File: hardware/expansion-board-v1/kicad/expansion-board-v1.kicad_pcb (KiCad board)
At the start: 4 copper layers, 100 x 62 mm, 156 parts, among them J1 PinHeader_2x20_P2.54mm_Vertic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, J2 U.FL_Hirose_U.FL-R-SMT-1_Vert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, J4 USB_C_Receptacle_HRO_TYPE-C-3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, J5 U.FL_Hirose_U.FL-R-SMT-1_Vert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, J6 U.FL_Hirose_U.FL-R-SMT-1_Vert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, J7 ANT_IFA_1090MHz, J8 U.FL_Hirose_U.FL-R-SMT-1_Vert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, Q2 SOT-23, Q3 SOT-23, Q4 SOT-23, Q5 SOT-23, SW1 SolderJumper-2_P1.3mm_Open_Pa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, SW2 SolderJumper-2_P1.3mm_Open_Pa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, U1 SOT-23-5, U10 QFN-48-1EP_7x7mm_P0.5mm_EP5.1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, U11 DFN-8-1EP_2x2mm_P0.5mm_EP0.86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, U12 SOT-363_SC-70-6, U13 AD8319_LFCSP-8-EP, U14 MSOP-8_3x3mm_P0.65mm, U15 SOT-23-6, U16 SOT-363_SC-70-6, U17 SOT-363_SC-70-6, U2 SOT-23-5, U3 SOT-23-5, U4 BNO085_LGA-28, U5 BMP388_LGA-10, U6 LGA-16_3x3mm_P0.5mm, U7 ATGM336H_LCC-18, U8 QFN-56-1EP_7x7mm_P0.4mm_EP3.2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, U9 SOIC-8_5.3x5.3mm_P1.27mm, Y1 Crystal_SMD_3225-4Pin_3.2x2.5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, Y2 Crystal_SMD_3225-4Pin_3.2x2.5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, Y3 Crystal_SMD_3215-2Pin_3.2x1.5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

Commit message: feat(hw): 布局冻结为设计数据 + 丝印对齐机检 + 板名改 Avionics Board
## 布局所有权转移
区域装箱器的任务已完成——它把 152 个元件从零摆到可用起点。
用户人工精修了 81 个元件（把 CC1312R 去耦聚拢、978 直流侧贴近 J1 等，
装箱器摆不出来的判断）。精修后坐标即设计本身，不该再被算法覆盖。

  tools/export_placement.py  读 PCB → 行吸附 → 产出 PLACEMENT.py（只读源板）
  tools/PLACEMENT.py         156 元件 + 156 位号坐标，**设计数据不是生成物**
  gen_pcb.py / gen_silk.py   改为按 PLACEMENT.py 摆位；装箱与试位降级为新件兜底

往返验证：139/156 逐值一致，17 处差异恰为吸附项，无意外漂移。

## 对齐吸附（人工对不准，必须靠算法）
判据：同簇 = y 差 ≤0.35mm 且 x 间距 ≤12mm；目标取众数而非中位数
（多数已对齐、少数漂了，中位数会把对好的拽歪）。
实例：用户手拉 L14 行到 66.500，而 Q5 行是 66.553——肉眼差了 0.053mm。

## 新增三道丝印机检（这些问题此前靠人眼发现，漏过多次）
- 位号不得压在自己元件本体上（大件豁免）
- 同行 + 同高 + 同侧的位号绝对 y 必须一致
- 行对齐 pass 的每个候选位置都要过 压本体/压焊盘/压文字 三项

## 修掉的缺陷
- 冻结时把**失败状态**也固化：F.Fab 与"位号压本体"是算法状态不是设计意图，
  冻结导致永不重试（C62/C16/C17 因此永远没有位号）。改为只冻结成功项。
- 曾把行对齐写进 export_placement.py 盲改（那里没有障碍模型），
  把位号推到焊盘和丝印轮廓上（重叠 5→17、压铜 5→28）。对齐移入 gen_silk.py。
- C61/C66 两行下移 0.5mm：上一行本体底 94.33 与本行本体顶 95.72 净空仅 1.39mm，
  而位号需 0.5+1.1=1.6mm。

## 其它
- 板名 ADS-B Expansion → Avionics Board（功能已含 GNSS/IMU/BARO，不止 ADS-B）
- 背面丝印加 https://air.club
- J7 → ANT1（J 前缀属连接器，天线应用 ANT）
- tools/render.sh 出顶/底 3D + 分层 SVG + 装配图 PDF

状态：铜层 DRC 0 违例；丝印 2 出界 + 5 重叠；位号 156/156 全上板；布线未开始。
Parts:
- removed J7: ANT_IFA_1090MHz, ANT_IFA_1090MHz
- added ANT1: ANT_IFA_1090MHz, ANT_IFA_1090MHz, F.Cu at (105.0, 57.8)
- moved C46 86.5 mm to (55.6, 68.0)
- moved R31 82.6 mm to (55.6, 65.6)
- moved C2 79.6 mm to (62.0, 98.3)
- moved J6 71.1 mm to (124.3, 62.1)
- moved C51 70.6 mm to (55.6, 84.5)
- moved R35 66.3 mm to (55.6, 82.3)
- moved C49 62.1 mm to (55.6, 79.9)
- moved U2 59.8 mm to (63.1, 93.3)
- moved U1 59.7 mm to (69.2, 93.3)
- moved U3 59.5 mm to (74.3, 93.3)
- moved C1 59.3 mm to (79.1, 93.3)
- moved R34 57.8 mm to (55.6, 77.5)
- moved C3 54.8 mm to (66.5, 98.3)
- moved C4 54.1 mm to (71.0, 98.3)
- moved R33 53.6 mm to (55.6, 75.1)
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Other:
- board text added: "(c) Pilot Kit"
- board text added: "1090 / 978 ADS-B + GNSS + IMU + BARO"
- board text added: "1090 EXT"
- board text added: "1090MHz IFA ANT"
- board text added: "978 UAT"
- board text added: "GNSS EXT"
- board text added: "GNSS INT"
- board text added: "Pilot Kit Avionics Board"
- board text added: "USB"
- board text added: "V1 2026-08"
- board text added: "https://air.club"

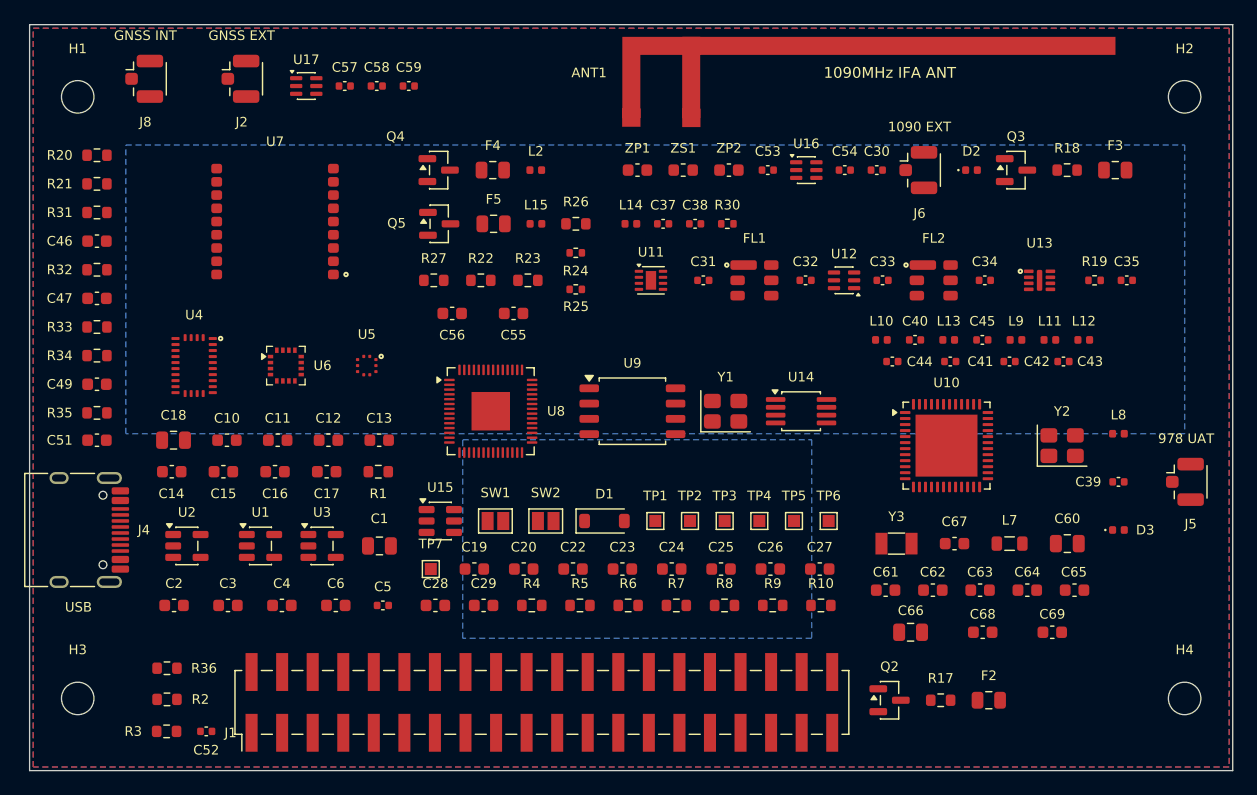
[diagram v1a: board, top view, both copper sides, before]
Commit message: chore(pcb): 重跑布线与渲染——可复现基线
跑 reroute.sh 全流程后的板子与渲染图。这是 DSN 规范化排序之后的第一版，
同样的输入必然得到同样的结果，可以作为后续改动的对照基准。

  走线 1302 段 / 过孔 398（F.Cu 934 / In2 231 / B.Cu 137）
  铜层 DRC  2 starved_thermal + 1 via_dangling（零短路、零间距违例）
  丝印 DRC  2 出界 + 12 重叠 + 1 压铜
  射频      151 段全在 F.Cu、0 过孔、In1 参考面 0 段走线
  天线      44.000mm

未连接 35 处 = 真缺线 22（射频 5、U8 相关 14）+ 断头铜 9 + 覆铜 4。
板子还不能用：U8(RP2040) 与 U10(CC1312R) 的内核供电/晶振/Flash 仍有断点，
两颗主控都起不来。U8 那 14 处是横跨所有尝试的不变量，是真正的瓶颈。
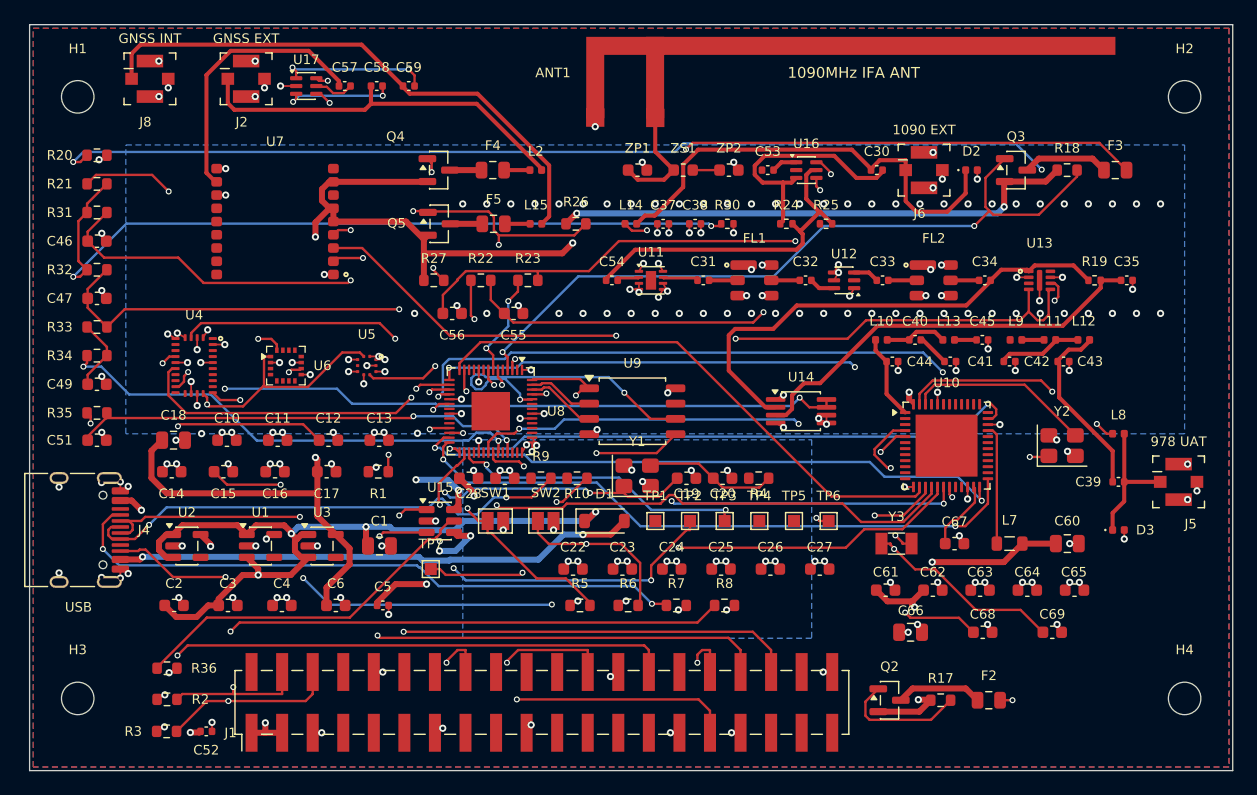
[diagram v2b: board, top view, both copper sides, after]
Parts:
- J2, J5, J6, J8: value U.FL_Hirose_U.FL-R-SMT-1_Vertical -> IPEX_ANT_SMD_2.6x2.6; footprint U.FL_Hirose_U.FL-R-SMT-1_Vertical -> IPEX_ANT_SMD_2.6x2.6
- moved R10 22.9 mm to (95.5, 87.7)
- moved R9 22.0 mm to (92.5, 87.7)
- moved R4 21.6 mm to (110.6, 87.7)
- moved R25 21.5 mm to (116.2, 66.5)
- moved C54 21.4 mm to (98.4, 71.2)
- moved C19 19.2 mm to (104.6, 87.7)
- moved C20 18.2 mm to (107.6, 87.7)
- moved R24 17.7 mm to (112.9, 66.5)
- moved C28 10.9 mm to (86.5, 87.7)
- moved C29 10.7 mm to (89.5, 87.7)
- moved Y1 9.10 mm to (100.5, 87.5)
- moved ANT1 3.00 mm to (102.0, 57.8)
- moved J5 1.00 mm to (145.5, 88.0)
- turned U8 to -90 degrees
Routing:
- net 3V3_GNSS: track 0.00 -> 187.0 mm, vias 0 -> 6
- net RF_DET_OUT: track 0.00 -> 121.1 mm, vias 0 -> 4
- net GND: track 0.00 -> 101.5 mm, vias 0 -> 190
- net DET_TADJ: track 0.00 -> 96.8 mm, vias 0 -> 3
- net VCC_5V: track 0.00 -> 80.5 mm, vias 0 -> 5
- net AD8313_VOUT: track 0.00 -> 77.9 mm, vias 0 -> 3
- net SUBG_CSN: track 0.00 -> 74.3 mm, vias 0 -> 2
- net GNSS_PPS: track 0.00 -> 69.3 mm, vias 0 -> 2
- net GNSS_TXD: track 0.00 -> 68.6 mm, vias 0 -> 2
- net IMU_INT: track 0.00 -> 67.6 mm, vias 0 -> 2
- net 3V3_RF: track 0.00 -> 63.6 mm, vias 0 -> 17
- net BIAS_EN_1090: track 0.00 -> 61.4 mm, vias 0 -> 2
- net GNSS_RXD: track 0.00 -> 60.2 mm, vias 0 -> 2
- net SUBG_IRQ: track 0.00 -> 59.3 mm, vias 0 -> 3
- net I2C_SCL: track 0.00 -> 58.9 mm, vias 0 -> 2
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
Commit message: perf(pcb): 默认线宽 0.2→0.15 + 收窄 RP_1V1 电源岛，真缺线 22→11
有了可复现的流水线（见 5cf5d0b），终于能可信地做单变量对照。逐项实测：

  变量                          未连接  缺线  射频  U8相关  铜层DRC
  基线 线宽0.20 间距0.15 大岛       35    22    5     14      3
  放开 In1 当走线层                38    23    4     13      2
  线宽0.15 间距0.127              31    15    5      6     82
  线宽0.15 间距0.15               30    13    4      5     19
  线宽0.13 间距0.15 小岛           36    24    6     10      9
  线宽0.15 间距0.15 小岛 ← 采用     26    13    3      6      4

结论：

1) 线宽是真凶，不是间距。U8 是 QFN-56、0.4mm pitch，中心到邻脚边缘只有
   0.3mm，要塞下一根线需 线宽/2 + 间距 ≤ 0.3。0.20/0.15 用掉 0.25 几乎卡死，
   0.15/0.15 只用 0.225。改这一个数就把 U8 的扇出断点从 14 处压到 5 处。

2) 更细不是单调更好。0.13 反而退回 24 处缺线，比 0.15 差一倍。

3) 间距 0.15 是硬下限。孔到铜要求 0.25mm，而孔间距 = 铜间距 + 过孔环宽
   (0.5焊盘−0.3孔)/2 = 铜间距 + 0.1。降到 0.127 会差 0.021mm，实测炸出
   61 条 hole_clearance。

4) 放开 In1 确认无用（38 vs 35）。freerouting 只是把 179 段甩到 In1、
   B.Cu 反而只剩 17 段——它不缺层，是在重新分配。而代价是射频参考面被切碎。
   In1 继续锁死。

5) RP_1V1 电源岛收窄到 11x4.7mm：原来 478mm² 被走线切成 11 块碎铜
   （isolated_copper x11），而这个网络全网只有 5 个焊盘、挤在 7x6mm 内。
   收窄后碎铜清零、未连接再降 4 处。
   注：更早一次"收窄更差"的结论是在 DSN 规范化排序之前测的，不可信，已推翻。

当前状态：
  走线 1438 段 / 过孔 405（F.Cu 1019 / In2 232 / B.Cu 187）
  铜层 DRC 只剩 4 个悬空过孔——零短路、零间距违例、零孤立铜
  射频 172 段全在 F.Cu、0 过孔、In1 参考面 0 段走线
  未连接 26 = 真缺线 11（射频 3）+ 断头铜 10 + 覆铜 5

板子仍不可用：RP_1V1 还差 3 处（RP2040 内核供电）、SUBG_VDDR 1 处
（CC1312R 射频供电），两颗主控还起不来。
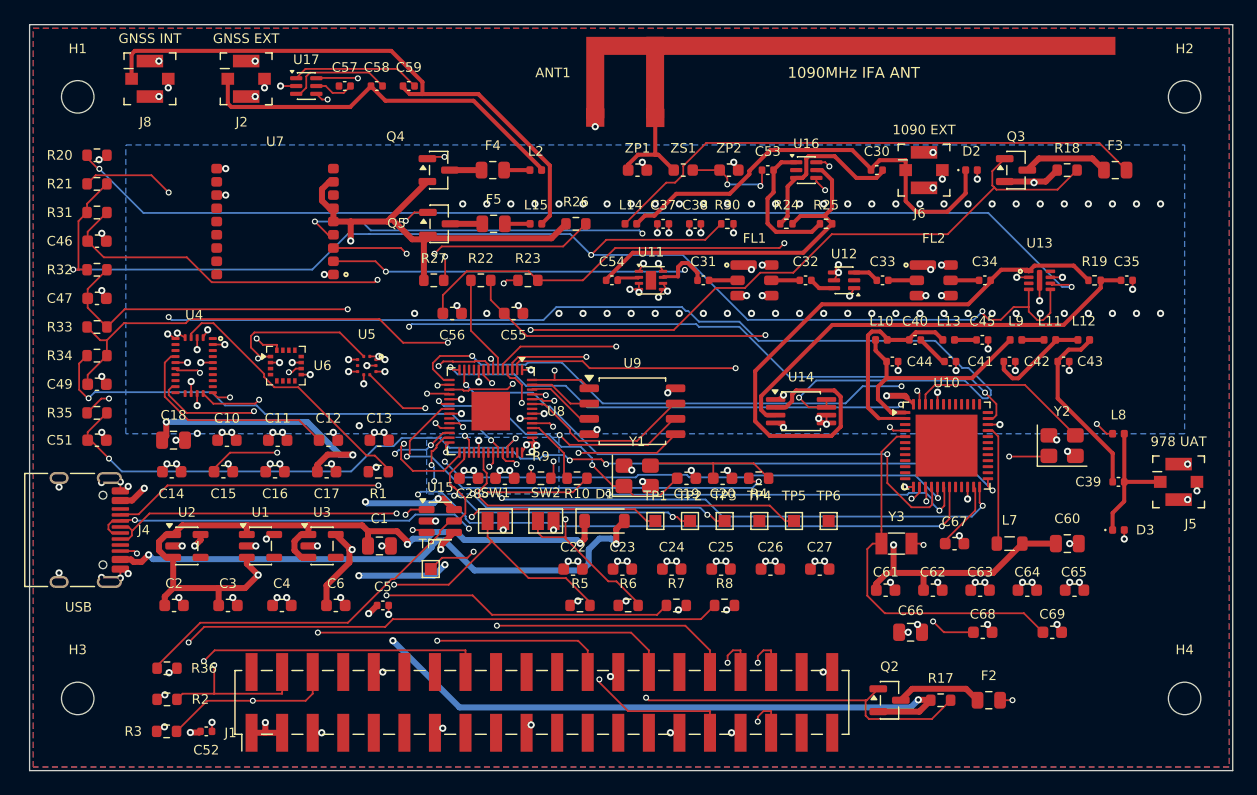
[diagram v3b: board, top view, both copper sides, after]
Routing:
- net BIAS_EN_978: track 10.6 -> 69.6 mm, vias 0 -> 2
- net ADSB_TXD: track 0.00 -> 52.7 mm, vias 0 -> 2
- net LEVEL_BIAS: track 6.10 -> 50.8 mm, vias 0 -> 2
- net RP_XOUT: track 0.00 -> 37.3 mm, vias 0 -> 2
- net DEMOD3: track 37.1 -> 0.00 mm, vias 3 -> 0
- net AD8313_VOUT: track 77.9 -> 110.7 mm
- net DEMOD2: track 0.00 -> 31.1 mm
- net SWCLK: track 0.00 -> 25.4 mm, vias 0 -> 2
- net SUBG_CSN: track 74.3 -> 51.6 mm, vias 2 -> 3
- net GNSS_RF_IN: track 22.6 -> 0.00 mm
- net SUBG_RESET: track 49.4 -> 70.7 mm, vias 2 -> 3
- net USB_DP: track 41.6 -> 61.0 mm
- net 3V3_GNSS: track 187.0 -> 204.3 mm, vias 6 -> 7
- net RP_RUN: track 21.9 -> 38.4 mm, vias 2 -> 3
- net ANT_SEL_GNSS_B: track 23.5 -> 38.8 mm, vias 3 -> 4
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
